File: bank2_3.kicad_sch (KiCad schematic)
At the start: 1 part, among them U1 ECP5-BGA256

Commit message: schematic wip
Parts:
- added C5 (x2): 1nF, Capacitor_SMD:C_0402_1005Metric, symbol Device:C
- added R24: 1k, Resistor_SMD:R_0402_1005Metric, symbol Device:R
- added R38: 10k, Resistor_SMD:R_0402_1005Metric, symbol Device:R
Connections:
- net GND: now also C5.2, C5.2
- net ADC_IN+: now reaches U1.D16 (PR8A)
- net ADC_IN+: now also C5.1, R24.2
- net ADC_IN-: now reaches U1.E15 (PR8B)
- net ADC_IN-: now also C5.1, R38.2
- net TX_XCVR.~{SHDN}: now reaches U1.E16 (PR11D)
- net ADC_PWM_OUT: now reaches U1.F15 (PR11C)
- net ADC_PWM_OUT: now also R38.1
- net TX_XCVR.B7: now reaches U1.F16 (PR14A)
- net TX_XCVR.B5: now reaches U1.G14 (PR14C)
- net TX_XCVR.B6: now reaches U1.G15 (PR14B)
- net TX_XCVR.~{CS}: now reaches U1.G16 (PR20A)
- net TX_XCVR.B3: now reaches U1.H12 (PR17A)
- net TX_XCVR.B2: now reaches U1.H13 (PR17B)
- net TX_XCVR.B4: now reaches U1.H14 (PR14D)
- net TX_XCVR.SCLK: now reaches U1.H15 (PR20B)
- net TX_XCVR.B1: now reaches U1.J13 (PR17C)
- net 3V3TX_EN: now reaches U1.J14 (PR20C)
- net TX_XCVR.RXHP: now reaches U1.J15 (PR23B)
- net FPGA_CLK: now reaches U1.J16 (PR23A)
- net TX_XCVR.DIN: now reaches U1.K14 (PR20D)
- net TX_XCVR.LD: now reaches U1.K15 (PR23D)
- net TX_XCVR.RXTX: now reaches U1.K16 (PR23C)
- net LED4: now reaches U1.K13 (PR29A)
- net LED5: now reaches U1.L13 (PR29C)
- net CONTROL_PHY.CLK renamed PHY.CLK
- net CONTROL_PHY.DATA0 renamed PHY.DATA0
- net CONTROL_PHY.DATA1 renamed PHY.DATA1
- net CONTROL_PHY.DATA2 renamed PHY.DATA2
- net CONTROL_PHY.DATA3 renamed PHY.DATA3
- net CONTROL_PHY.DATA4 renamed PHY.DATA4
- net CONTROL_PHY.DATA5 renamed PHY.DATA5
- net CONTROL_PHY.DATA6 renamed PHY.DATA6
- net CONTROL_PHY.DATA7 renamed PHY.DATA7
- net CONTROL_PHY.DIR renamed PHY.DIR
- net CONTROL_PHY.NXT renamed PHY.NXT
- net CONTROL_PHY.STP renamed PHY.STP
- net CONTROL_PHY.~{RESET} renamed PHY.~{RESET}
- net MEZZANINE10 renamed TX_MIX_CTRL.SDATA
- net MEZZANINE11 renamed TX_MIX_CTRL.SCLK
- net MEZZANINE12 renamed ~{TX_MIX_BYPASS}
- net MEZZANINE13: no longer names the net of U1.G12 (PR11A)
- net MEZZANINE18 renamed TX_MIX_CTRL.~{RESET}
- net MEZZANINE19 renamed TX_MIX_CTRL.~{EN}
- net MEZZANINE20 renamed TX_MIX_CTRL.FM
- net MEZZANINE21 renamed TX_MIX_CTRL.LD
- net MEZZANINE8 renamed TX_MIX_CTRL.MODE
- net MEZZANINE9 renamed TX_MIX_CTRL.ENBL
- net ~{BTN_USER} renamed LED6
- new net TX_XCVR.RSSI: R24.1
- no-connect marks 23 -> 3

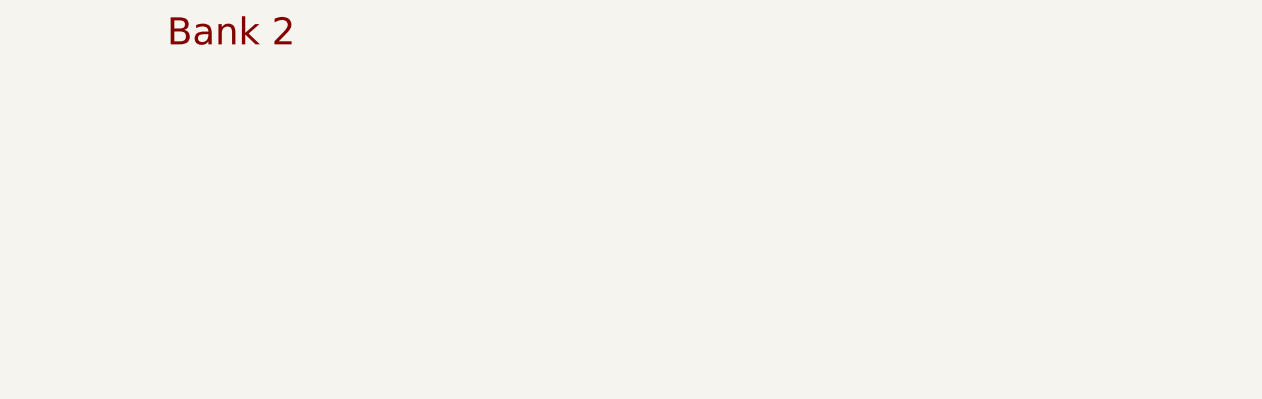
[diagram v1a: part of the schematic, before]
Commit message: add regulator for analog 3.3 V supply
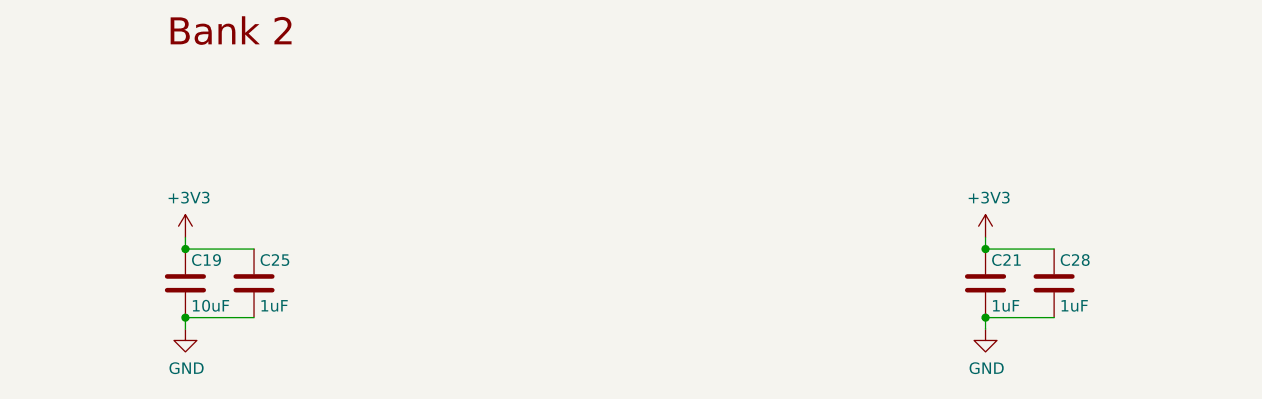
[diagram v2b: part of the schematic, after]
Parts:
- added C19: 10uF, Capacitor_SMD:C_0603_1608Metric, symbol Device:C
- added C21, C25, C28: 1uF, Capacitor_SMD:C_0402_1005Metric, symbol Device:C
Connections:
- net +3V3: now also C19.1, C21.1, C25.1, C28.1
- net GND: now also C19.2, C21.2, C25.2, C28.2

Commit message: layout wip
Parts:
- C5: footprint Capacitor_SMD:C_0402_1005Metric -> Capacitor_SMD:C_0201_0603Metric; Manufacturer Samsung -> Murata; Part Number CL05B102KB5NNNC -> GRM033R71E102KA01D; Substitution any equivalent -> GRM033R71E102KA01*
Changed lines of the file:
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@@
       (effects (font (size 1.27 1.27)) (justify left))
     )
-    (property "Footprint" "Capacitor_SMD:C_0402_1005Metric" (at 116.5352 130.81 0)
+    (property "Footprint" "Capacitor_SMD:C_0201_0603Metric" (at 116.5352 130.81 0)
       (effects (font (size 1.27 1.27)) hide)
     )
@@
       (effects (font (size 1.27 1.27)) hide)
     )
-    (property "Part Number" "CL05B102KB5NNNC" (at 115.57 127 0)
-      (effects (font (size 1.27 1.27)) hide)
-    )
-    (property "Substitution" "any equivalent" (at 115.57 127 0)
-      (effects (font (size 1.27 1.27)) hide)
-    )
-    (property "Description" "CAP CER 1000PF 50V X7R 0402" (at 115.57 127 0)
-      (effects (font (size 1.27 1.27)) hide)
-    )
-    (property "Manufacturer" "Samsung" (at 115.57 127 0)
+    (property "Part Number" "GRM033R71E102KA01D" (at 115.57 127 0)
+      (effects (font (size 1.27 1.27)) hide)
+    )
+    (property "Substitution" "GRM033R71E102KA01*" (at 115.57 127 0)
+      (effects (font (size 1.27 1.27)) hide)
+    )
+    (property "Description" "CAP CER 1000PF 25V X7R 0201" (at 115.57 127 0)
+      (effects (font (size 1.27 1.27)) hide)
+    )
+    (property "Manufacturer" "Murata" (at 115.57 127 0)
       (effects (font (size 1.27 1.27)) hide)
     )
@@
       (effects (font (size 1.27 1.27)) (justify left))
     )
-    (property "Footprint" "Capacitor_SMD:C_0402_1005Metric" (at 119.0752 107.95 0)
+    (property "Footprint" "Capacitor_SMD:C_0201_0603Metric" (at 119.0752 107.95 0)
       (effects (font (size 1.27 1.27)) hide)
     )
@@
       (effects (font (size 1.27 1.27)) hide)
     )
-    (property "Part Number" "CL05B102KB5NNNC" (at 118.11 104.14 0)
-      (effects (font (size 1.27 1.27)) hide)
-    )
-    (property "Substitution" "any equivalent" (at 118.11 104.14 0)
-      (effects (font (size 1.27 1.27)) hide)
-    )
-    (property "Description" "CAP CER 1000PF 50V X7R 0402" (at 118.11 104.14 0)
-      (effects (font (size 1.27 1.27)) hide)
-    )
-    (property "Manufacturer" "Samsung" (at 118.11 104.14 0)
-      (effects (font (size 1.27 1.27)) hide)
-    )
+    (property "Part Number" "GRM033R71E102KA01D" (at 118.11 104.14 0)
+      (effects (font (size 1.27 1.27)) hide)
+    )
+    (property "Substitution" "GRM033R71E102KA01*" (at 118.11 104.14 0)
+      (effects (font (size 1.27 1.27)) hide)
+    )
+    (property "Description" "CAP CER 1000PF 25V X7R 0201" (at 118.11 104.14 0)
+      (effects (font (size 1.27 1.27)) hide)
+    )
+    (property "Manufacturer" "Murata" (at 118.11 104.14 0)
+      (effects (font (size 1.27 1.27)) hide)
+    )

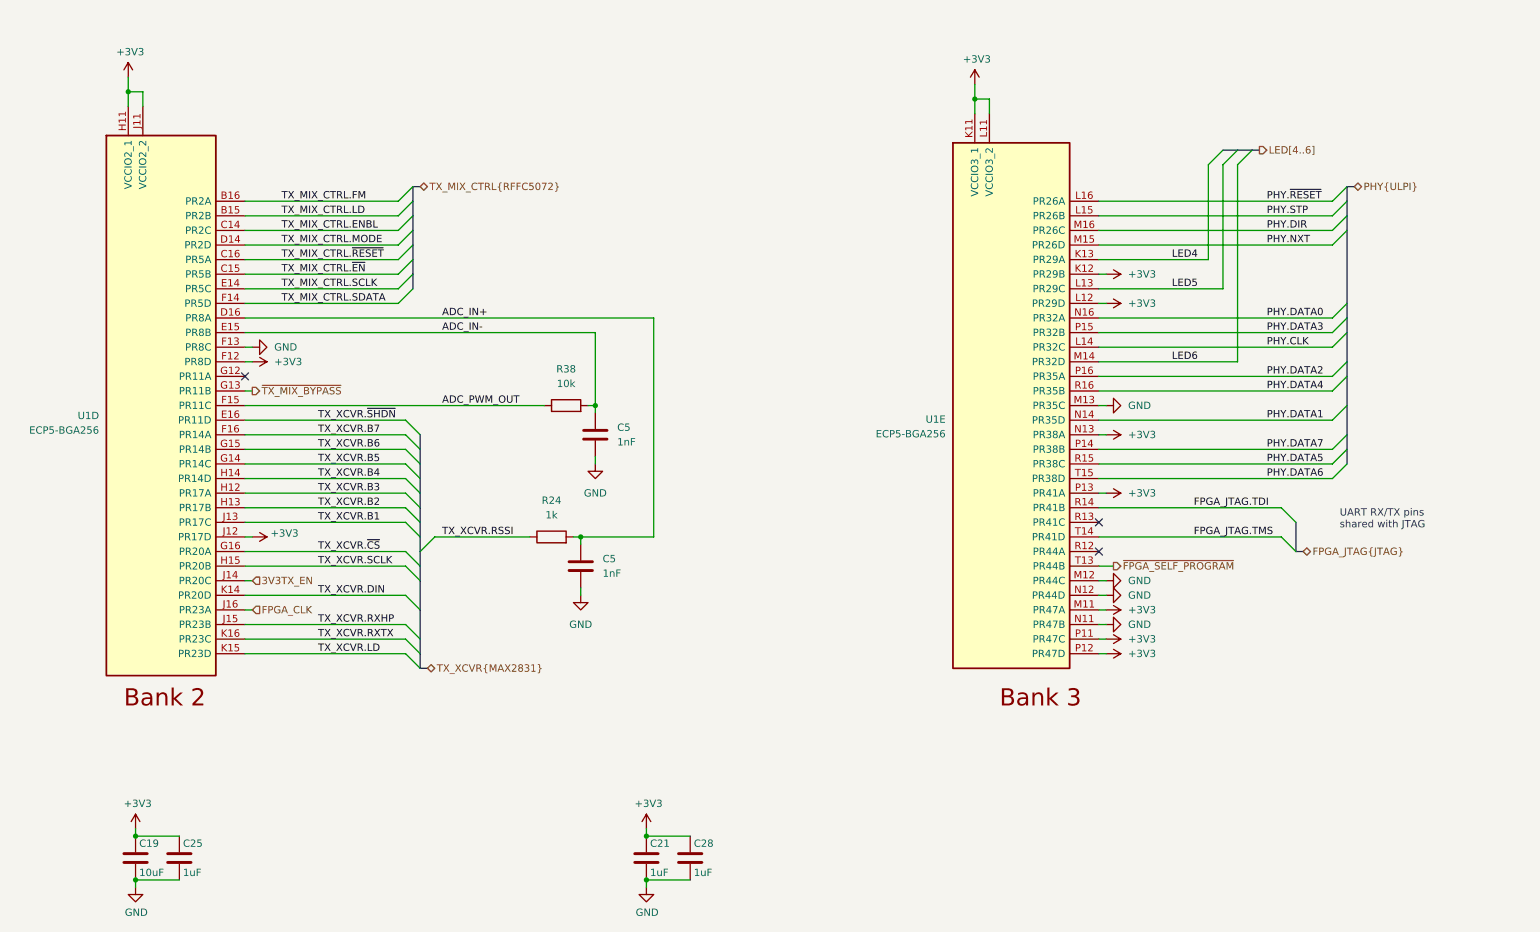
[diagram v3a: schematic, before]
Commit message: layout wip: radio FPGA connections and clocks
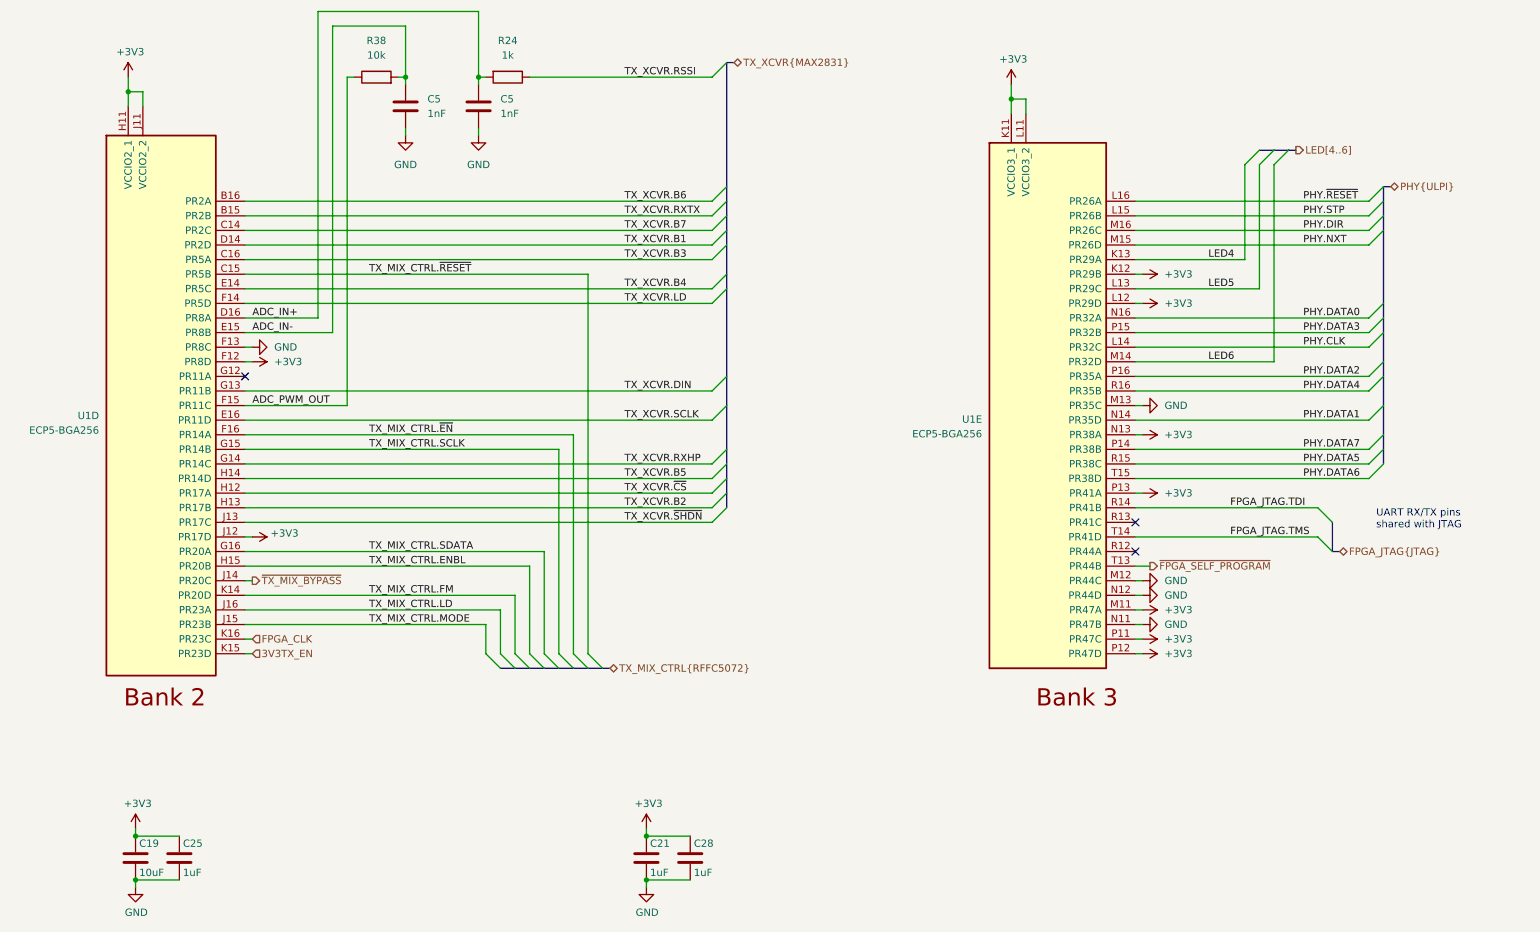
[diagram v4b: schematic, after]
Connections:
- net 3V3TX_EN: now also U1.K15 (PR23D); no longer U1.J14 (PR20C)
- net FPGA_CLK: now also U1.K16 (PR23C); no longer U1.J16 (PR23A)
- net TX_MIX_CTRL.ENBL: now also U1.H15 (PR20B); no longer U1.C14 (PR2C)
- net TX_MIX_CTRL.FM: now also U1.K14 (PR20D); no longer U1.B16 (PR2A)
- net TX_MIX_CTRL.LD: now also U1.J16 (PR23A); no longer U1.B15 (PR2B)
- net TX_MIX_CTRL.MODE: now also U1.J15 (PR23B); no longer U1.D14 (PR2D)
- net TX_MIX_CTRL.SCLK: now also U1.G15 (PR14B); no longer U1.E14 (PR5C)
- net TX_MIX_CTRL.SDATA: now also U1.G16 (PR20A); no longer U1.F14 (PR5D)
- net TX_MIX_CTRL.~{EN}: now also U1.F16 (PR14A); no longer U1.C15 (PR5B)
- net TX_MIX_CTRL.~{RESET}: now also U1.C15 (PR5B); no longer U1.C16 (PR5A)
- net TX_XCVR.B1: now also U1.D14 (PR2D); no longer U1.J13 (PR17C)
- net TX_XCVR.B3: now also U1.C16 (PR5A); no longer U1.H12 (PR17A)
- net TX_XCVR.B4: now also U1.E14 (PR5C); no longer U1.H14 (PR14D)
- net TX_XCVR.B5: now also U1.H14 (PR14D); no longer U1.G14 (PR14C)
- net TX_XCVR.B6: now also U1.B16 (PR2A); no longer U1.G15 (PR14B)
- net TX_XCVR.B7: now also U1.C14 (PR2C); no longer U1.F16 (PR14A)
- net TX_XCVR.DIN: now also U1.G13 (PR11B); no longer U1.K14 (PR20D)
- net TX_XCVR.LD: now also U1.F14 (PR5D); no longer U1.K15 (PR23D)
- net TX_XCVR.RXHP: now also U1.G14 (PR14C); no longer U1.J15 (PR23B)
- net TX_XCVR.RXTX: now also U1.B15 (PR2B); no longer U1.K16 (PR23C)
- net TX_XCVR.SCLK: now also U1.E16 (PR11D); no longer U1.H15 (PR20B)
- net TX_XCVR.~{CS}: now also U1.H12 (PR17A); no longer U1.G16 (PR20A)
- net TX_XCVR.~{SHDN}: now also U1.J13 (PR17C); no longer U1.E16 (PR11D)
- net ~{TX_MIX_BYPASS}: now also U1.J14 (PR20C); no longer U1.G13 (PR11B)
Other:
- moved on the sheet: C5, R24, R38, U1E

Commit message: more layout wip
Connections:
- net 3V3TX_EN: now also U1.J16 (PR23A); no longer U1.K15 (PR23D)
- net TX_MIX_CTRL.LD: now also U1.K15 (PR23D); no longer U1.J16 (PR23A)
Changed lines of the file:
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@@
   (no_connect (at 57.15 93.98))
   (no_connect (at 212.09 124.46))
-  (bus_entry (at 111.76 144.78) (size -2.54 -2.54)
-    (stroke (width 0) (type default))
-  )
-  (bus_entry (at 106.68 144.78) (size -2.54 -2.54)
+  (bus_entry (at 111.76 149.86) (size -2.54 -2.54)
+    (stroke (width 0) (type default))
+  )
+  (bus_entry (at 106.68 149.86) (size -2.54 -2.54)
     (stroke (width 0) (type default))
   )
@@
     (stroke (width 0) (type default))
   )
-  (bus_entry (at 104.14 144.78) (size -2.54 -2.54)
+  (bus_entry (at 104.14 149.86) (size -2.54 -2.54)
     (stroke (width 0) (type default))
   )
@@
     (stroke (width 0) (type default))
   )
-  (bus_entry (at 116.84 144.78) (size -2.54 -2.54)
+  (bus_entry (at 116.84 149.86) (size -2.54 -2.54)
     (stroke (width 0) (type default))
   )
@@
     (stroke (width 0) (type default))
   )
-  (bus_entry (at 114.3 144.78) (size -2.54 -2.54)
+  (bus_entry (at 114.3 149.86) (size -2.54 -2.54)
     (stroke (width 0) (type default))
   )
@@
     (stroke (width 0) (type default))
   )
-  (bus_entry (at 109.22 144.78) (size -2.54 -2.54)
+  (bus_entry (at 109.22 149.86) (size -2.54 -2.54)
     (stroke (width 0) (type default))
   )
@@
     (stroke (width 0) (type default))
   )
-  (bus_entry (at 101.6 144.78) (size -2.54 -2.54)
+  (bus_entry (at 101.6 149.86) (size -2.54 -2.54)
     (stroke (width 0) (type default))
   )
@@
     (stroke (width 0) (type default))
   )
-  (bus_entry (at 119.38 144.78) (size -2.54 -2.54)
+  (bus_entry (at 119.38 149.86) (size -2.54 -2.54)
     (stroke (width 0) (type default))
   )
@@
     (stroke (width 0) (type default))
   )
-  (bus (pts (xy 106.68 144.78) (xy 109.22 144.78))
+  (bus (pts (xy 106.68 149.86) (xy 109.22 149.86))
     (stroke (width 0) (type default))
   )
@@
     (stroke (width 0) (type default))
   )
-  (bus (pts (xy 109.22 144.78) (xy 111.76 144.78))
+  (bus (pts (xy 109.22 149.86) (xy 111.76 149.86))
     (stroke (width 0) (type default))
   )
@@
     (stroke (width 0) (type default))
   )
-  (wire (pts (xy 109.22 124.46) (xy 109.22 142.24))
+  (wire (pts (xy 109.22 124.46) (xy 109.22 147.32))
     (stroke (width 0) (type default))
   )
@@
     (stroke (width 0) (type default))
   )
-  (wire (pts (xy 114.3 104.14) (xy 114.3 142.24))
+  (wire (pts (xy 114.3 104.14) (xy 114.3 147.32))
     (stroke (width 0) (type default))
   )
@@
     (stroke (width 0) (type default))
   )
-  (bus (pts (xy 116.84 144.78) (xy 119.38 144.78))
+  (bus (pts (xy 116.84 149.86) (xy 119.38 149.86))
     (stroke (width 0) (type default))
   )
@@
     (stroke (width 0) (type default))
   )
-  (wire (pts (xy 57.15 142.24) (xy 58.42 142.24))
+  (wire (pts (xy 57.15 142.24) (xy 99.06 142.24))
     (stroke (width 0) (type default))
   )
@@
     (stroke (width 0) (type default))
   )
-  (wire (pts (xy 57.15 137.16) (xy 99.06 137.16))
+  (wire (pts (xy 57.15 137.16) (xy 101.6 137.16))
     (stroke (width 0) (type default))
   )
@@
     (stroke (width 0) (type default))
   )
-  (bus (pts (xy 101.6 144.78) (xy 104.14 144.78))
+  (bus (pts (xy 101.6 149.86) (xy 104.14 149.86))
     (stroke (width 0) (type default))
   )
@@
     (stroke (width 0) (type default))
   )
-  (bus (pts (xy 114.3 144.78) (xy 116.84 144.78))
+  (bus (pts (xy 114.3 149.86) (xy 116.84 149.86))
     (stroke (width 0) (type default))
   )
@@
     (stroke (width 0) (type default))
   )
-  (wire (pts (xy 57.15 134.62) (xy 101.6 134.62))
-    (stroke (width 0) (type default))
-  )
   (wire (pts (xy 97.79 30.48) (xy 69.85 30.48))
     (stroke (width 0) (type default))
@@
     (stroke (width 0) (type default))
   )
-  (wire (pts (xy 111.76 142.24) (xy 111.76 106.68))
+  (wire (pts (xy 111.76 147.32) (xy 111.76 106.68))
     (stroke (width 0) (type default))
   )
@@
     (stroke (width 0) (type default))
   )
-  (wire (pts (xy 101.6 142.24) (xy 101.6 134.62))
-    (stroke (width 0) (type default))
-  )
   (wire (pts (xy 57.15 91.44) (xy 58.42 91.44))
     (stroke (width 0) (type default))
@@
     (stroke (width 0) (type default))
   )
-  (wire (pts (xy 116.84 76.2) (xy 116.84 142.24))
+  (wire (pts (xy 116.84 76.2) (xy 116.84 147.32))
     (stroke (width 0) (type default))
   )
@@
     (stroke (width 0) (type default))
   )
-  (bus (pts (xy 120.65 144.78) (xy 119.38 144.78))
+  (wire (pts (xy 101.6 137.16) (xy 101.6 147.32))
+    (stroke (width 0) (type default))
+  )
+  (bus (pts (xy 120.65 149.86) (xy 119.38 149.86))
     (stroke (width 0) (type default))
   )
@@
     (stroke (width 0) (type default))
   )
+  (wire (pts (xy 99.06 142.24) (xy 99.06 147.32))
+    (stroke (width 0) (type default))
+  )
   (wire (pts (xy 57.15 129.54) (xy 58.42 129.54))
     (stroke (width 0) (type default))
@@
     (stroke (width 0) (type default))
   )
-  (wire (pts (xy 104.14 132.08) (xy 104.14 142.24))
-    (stroke (width 0) (type default))
-  )
-  (bus (pts (xy 104.14 144.78) (xy 106.68 144.78))
+  (wire (pts (xy 104.14 132.08) (xy 104.14 147.32))
+    (stroke (width 0) (type default))
+  )
+  (bus (pts (xy 104.14 149.86) (xy 106.68 149.86))
     (stroke (width 0) (type default))
   )
@@
     (stroke (width 0) (type default))
   )
-  (wire (pts (xy 99.06 137.16) (xy 99.06 142.24))
-    (stroke (width 0) (type default))
-  )
-  (bus (pts (xy 111.76 144.78) (xy 114.3 144.78))
+  (bus (pts (xy 111.76 149.86) (xy 114.3 149.86))
     (stroke (width 0) (type default))
   )
@@
     (stroke (width 0) (type default))
   )
+  (wire (pts (xy 57.15 134.62) (xy 58.42 134.62))
+    (stroke (width 0) (type default))
+  )
   (bus (pts (xy 240.03 54.61) (xy 238.76 54.61))
     (stroke (width 0) (type default))
@@
     (stroke (width 0) (type default))
   )
-  (wire (pts (xy 106.68 142.24) (xy 106.68 127))
+  (wire (pts (xy 106.68 147.32) (xy 106.68 127))
     (stroke (width 0) (type default))
   )
@@
     (effects (font (size 1.27 1.27)) (justify left bottom))
   )
-  (label "TX_MIX_CTRL.LD" (at 78.74 134.62 0) (fields_autoplaced)
+  (label "TX_MIX_CTRL.LD" (at 78.74 142.24 0) (fields_autoplaced)
     (effects (font (size 1.27 1.27)) (justify left bottom))
   )
@@
     (effects (font (size 1.27 1.27)) (justify left))
   )
-  (hierarchical_label "TX_MIX_CTRL{RFFC5072}" (shape bidirectional) (at 120.65 144.78 0) (fields_autoplaced)
+  (hierarchical_label "TX_MIX_CTRL{RFFC5072}" (shape bidirectional) (at 120.65 149.86 0) (fields_autoplaced)
     (effects (font (size 1.27 1.27)) (justify left))
   )
@@
     (effects (font (size 1.27 1.27)) (justify left))
   )
-  (hierarchical_label "3V3TX_EN" (shape input) (at 58.42 142.24 0) (fields_autoplaced)
+  (hierarchical_label "3V3TX_EN" (shape input) (at 58.42 134.62 0) (fields_autoplaced)
     (effects (font (size 1.27 1.27)) (justify left))
   )
